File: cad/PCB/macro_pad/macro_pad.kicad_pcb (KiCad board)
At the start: 2 copper layers, 82.3 x 100.8 mm, 39 parts, among them SW1 SW_Push, SW10 SW_Push, SW11 SW_Push, SW12 SW_Push, SW13 SW_Push, SW14 SW_Push, SW15 SW_Push, SW16 SW_Push, SW17 RotaryEncoder_Switch, SW2 SW_Push, SW3 SW_Push, SW4 SW_Push, SW5 SW_Push, SW6 SW_Push, SW7 SW_Push, SW8 SW_Push, SW9 SW_Push, U1 XIAO-SAMD21-DIP

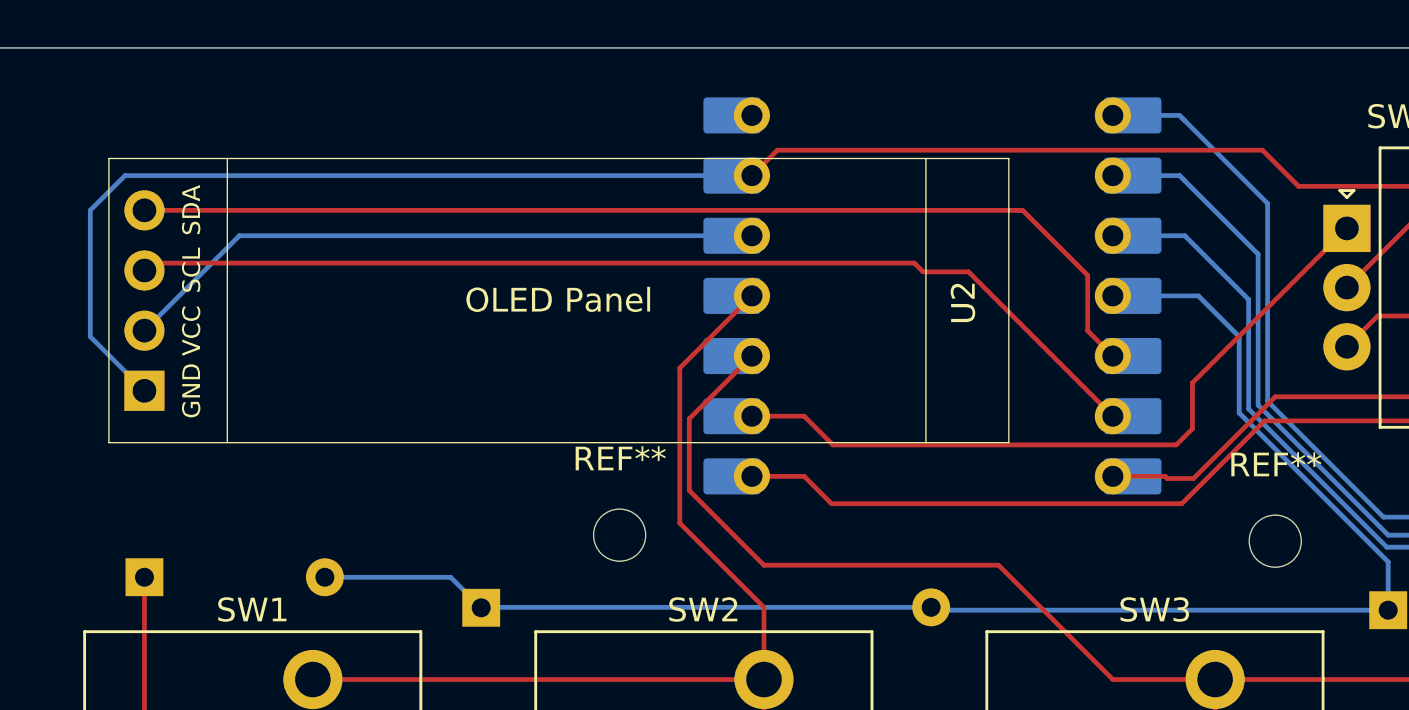
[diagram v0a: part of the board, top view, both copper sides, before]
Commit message: edited component placing added 3d models
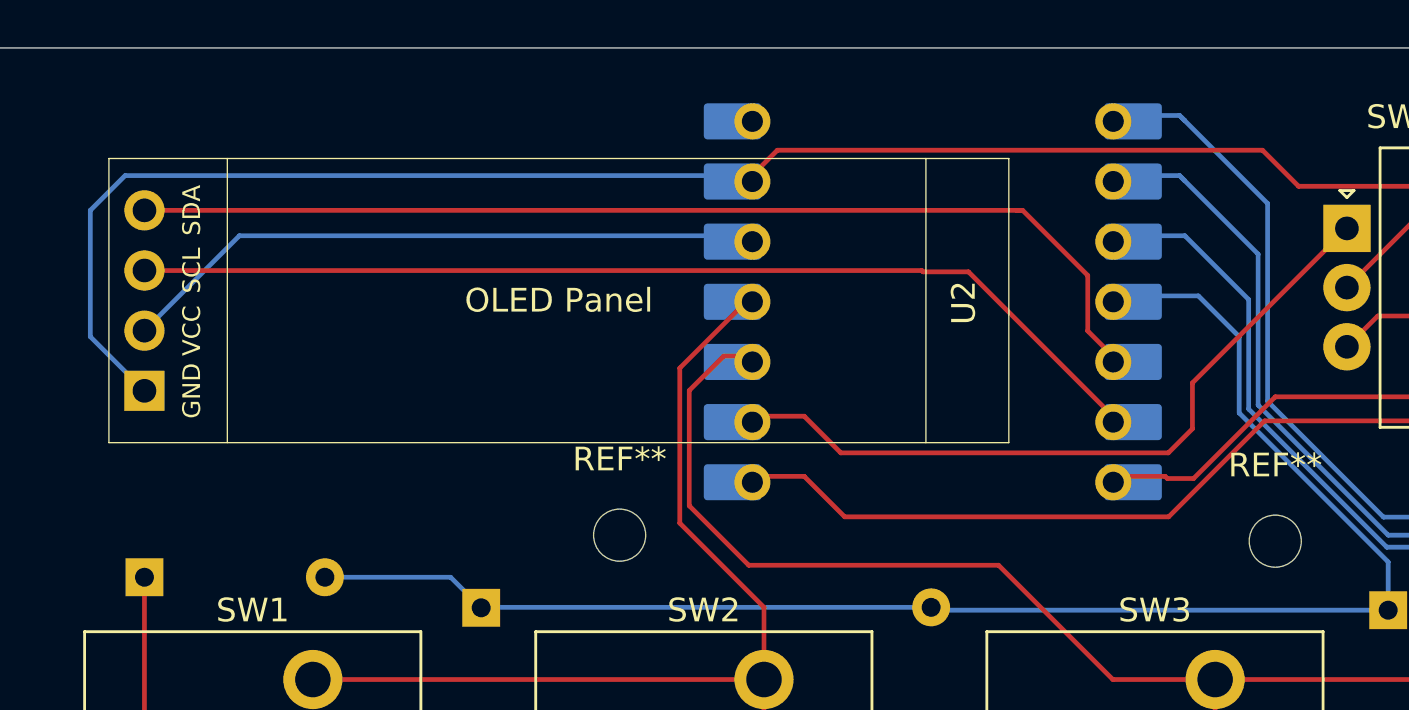
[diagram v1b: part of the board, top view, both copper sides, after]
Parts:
- moved U1 0.25 mm to (142.9, 74.2)
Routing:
- net Net-(U1-PA5_A9_D9_MISO): track 165.6 -> 166.7 mm
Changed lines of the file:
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@@
 			(outputformat 1)
 			(mirror no)
-			(drillshape 1)
+			(drillshape 0)
 			(scaleselection 1)
-			(outputdirectory "")
+			(outputdirectory "gerber/")
 		)
 	)
@@
 			(pintype "passive")
 		)
-		(model "${KICAD8_3DMODEL_DIR}/Rotary_Encoder.3dshapes/RotaryEncoder_Alps_EC11E-Switch_Vertical_H20mm.wrl"
+		(model "C:/Users/franc/Documents/KiCad/8.0/3dmodels/EC11_Rotary_Encoder_Switched.step"
 			(offset
-				(xyz 0 0 0)
+				(xyz 7.5 -2.5 0)
 			)
 			(scale
@@
 			)
 			(rotate
-				(xyz 0 0 0)
+				(xyz 0 0 90)
 			)
 		)
@@
 		(tags "Diode DO-35_SOD27 series Axial Horizontal pin pitch 7.62mm  length 4mm diameter 2mm")
 		(property "Reference" "D13"
-			(at 3.81 2.12 360)
+			(at 3.81 2.12 0)
 			(layer "B.SilkS")
 			(effects
@@
 		)
 		(property "Value" "D"
-			(at 3.81 -2.12 360)
+			(at 3.81 -2.12 0)
 			(layer "B.Fab")
 			(effects
@@
 		)
 		(fp_text user "K"
-			(at 0 1.8 360)
+			(at 0 1.8 0)
 			(layer "B.SilkS")
 			(effects
@@
 		)
 		(fp_text user "K"
-			(at 0 1.8 360)
+			(at 0 1.8 0)
 			(layer "B.Fab")
 			(effects
@@
 		)
 		(fp_text user "${REFERENCE}"
-			(at 4.11 0 360)
+			(at 4.11 0 0)
 			(layer "B.Fab")
 			(effects
@@
 		(tags "Diode DO-35_SOD27 series Axial Horizontal pin pitch 7.62mm  length 4mm diameter 2mm")
 		(property "Reference" "D1"
-			(at 3.81 2.12 360)
+			(at 3.81 2.12 0)
 			(layer "B.SilkS")
 			(effects
@@
 		)
 		(property "Value" "D"
-			(at 3.81 -2.12 360)
+			(at 3.81 -2.12 0)
 			(layer "B.Fab")
 			(effects
@@
 		)
 		(fp_text user "K"
-			(at 0 1.8 360)
+			(at 0 1.8 0)
 			(layer "B.SilkS")
 			(effects
@@
 		)
 		(fp_text user "K"
-			(at 0 1.8 360)
+			(at 0 1.8 0)
 			(layer "B.Fab")
 			(effects
@@
 		)
 		(fp_text user "${REFERENCE}"
-			(at 4.11 0 360)
+			(at 4.11 0 0)
 			(layer "B.Fab")
 			(effects
@@
 	(footprint "Seeed Studio XIAO Series Library:XIAO-SAMD21-DIP"
 		(layer "B.Cu")
-		(at 142.902 73.908 180)
+		(at 142.92 74.1575 180)
 		(property "Reference" "U1"
 			(at -8 12 0)
@@
 			)
 		)
-		(model "${AMZPATH}/3dmodels/AMz3D.3dshapes/Seeeduino XIAO SAMD21 v4.step"
+		(model "C:/Users/franc/Downloads/seeeduino-xiao-samd21-3d-model/Seeeduino XIAO SAMD21 v4.step"
 			(offset
 				(xyz 0 0 0)
@@
 			)
 			(rotate
-				(xyz 0 0 0)
+				(xyz 0 0 -90)
 			)
 		)
@@
 			)
 			(rotate
-				(xyz 0 0 90)
+				(xyz 90 0 90)
 			)
 		)
@@
 		(tags "Diode DO-35_SOD27 series Axial Horizontal pin pitch 7.62mm  length 4mm diameter 2mm")
 		(property "Reference" "D5"
-			(at 3.81 2.12 360)
+			(at 3.81 2.12 0)
 			(layer "B.SilkS")
 			(effects
@@
 		)
 		(property "Value" "D"
-			(at 3.81 -2.12 360)
+			(at 3.81 -2.12 0)
 			(layer "B.Fab")
 			(effects
@@
 		)
 		(fp_text user "K"
-			(at 0 1.8 360)
+			(at 0 1.8 0)
 			(layer "B.SilkS")
 			(effects
@@
 		)
 		(fp_text user "K"
-			(at 0 1.8 360)
+			(at 0 1.8 0)
 			(layer "B.Fab")
 			(effects
@@
 		)
 		(fp_text user "${REFERENCE}"
-			(at 4.11 0 360)
+			(at 4.11 0 0)
 			(layer "B.Fab")
 			(effects
@@
 		(tags "Diode DO-35_SOD27 series Axial Horizontal pin pitch 7.62mm  length 4mm diameter 2mm")
 		(property "Reference" "D9"
-			(at 3.81 2.12 360)
+			(at 3.81 2.12 0)
 			(layer "B.SilkS")
 			(effects
@@
 		)
 		(property "Value" "D"
-			(at 3.81 -2.12 360)
+			(at 3.81 -2.12 0)
 			(layer "B.Fab")
 			(effects
@@
 		)
 		(fp_text user "K"
-			(at 0 1.8 360)
+			(at 0 1.8 0)
 			(layer "B.SilkS")
 			(effects
@@
 		)
 		(fp_text user "K"
-			(at 0 1.8 360)
+			(at 0 1.8 0)
 			(layer "B.Fab")
 			(effects
@@
 		)
 		(fp_text user "${REFERENCE}"
-			(at 4.11 0 360)
+			(at 4.11 0 0)
 			(layer "B.Fab")
 			(effects
@@
 	)
 	(segment
+		(start 135.244 85.344)
+		(end 132.734 82.834)
+		(width 0.2)
+		(layer "F.Cu")
+		(net 20)
+	)
+	(segment
 		(start 154.94 128.27)
 		(end 154.94 147.32)
@@
 	)
 	(segment
-		(start 173.99 147.32)
-		(end 154.94 147.32)
+		(start 132.734 77.966)
+		(end 134.1895 76.5105)
 		(width 0.2)
 		(layer "F.Cu")
@@
 	)
 	(segment
-		(start 132.734 79.1585)
-		(end 135.382 76.5105)
+		(start 173.99 147.32)
+		(end 154.94 147.32)
 		(width 0.2)
 		(layer "F.Cu")
@@
 	)
 	(segment
-		(start 132.734 82.188)
-		(end 132.734 79.1585)
+		(start 173.99 90.17)
+		(end 154.94 90.17)
 		(width 0.2)
 		(layer "F.Cu")
@@
 	)
 	(segment
-		(start 173.99 90.17)
-		(end 154.94 90.17)
+		(start 150.622 90.17)
+		(end 145.796 85.344)
 		(width 0.2)
 		(layer "F.Cu")
@@
 	)
 	(segment
-		(start 135.89 85.344)
-		(end 132.734 82.188)
+		(start 145.796 85.344)
+		(end 135.244 85.344)
 		(width 0.2)
 		(layer "F.Cu")
@@
 	)
 	(segment
-		(start 150.622 90.17)
-		(end 145.796 85.344)
+		(start 134.1895 76.5105)
+		(end 135.382 76.5105)
 		(width 0.2)
 		(layer "F.Cu")
@@
 	)
 	(segment
-		(start 145.796 85.344)
-		(end 135.89 85.344)
+		(start 173.99 109.22)
+		(end 154.94 109.22)
 		(width 0.2)
 		(layer "F.Cu")
@@
 	)
 	(segment
-		(start 173.99 109.22)
-		(end 154.94 109.22)
+		(start 132.734 82.834)
+		(end 132.734 77.966)
 		(width 0.2)
 		(layer "F.Cu")
@@
 	)
 	(segment
-		(start 157.029686 79.248)
-		(end 153.533186 82.7445)
+		(start 175.494478 77.47)
+		(end 166.612 77.47)
 		(width 0.2)
 		(layer "F.Cu")
@@
 	)
 	(segment
-		(start 153.533186 82.7445)
-		(end 138.742 82.7445)
+		(start 164.834 79.248)
+		(end 157.029686 79.248)
 		(width 0.2)
 		(layer "F.Cu")
@@
 	)
 	(segment
-		(start 164.834 79.248)
-		(end 157.029686 79.248)
+		(start 160.506 76.12)
+		(end 161.806 74.82)
 		(width 0.2)
 		(layer "F.Cu")
@@
 	)
 	(segment
-		(start 175.544478 74.82)
-		(end 176.306 75.581522)
+		(start 176.306 76.658478)
+		(end 175.494478 77.47)
 		(width 0.2)
 		(layer "F.Cu")
@@
 	)
 	(segment
-		(start 160.506 76.12)
-		(end 161.806 74.82)
+		(start 166.612 77.47)
+		(end 164.834 79.248)
 		(width 0.2)
 		(layer "F.Cu")
@@
 	)
 	(segment
-		(start 137.588 81.5905)
-		(end 135.382 81.5905)
+		(start 175.544478 74.82)
+		(end 176.306 75.581522)
 		(width 0.2)
 		(layer "F.Cu")
@@
 	)
 	(segment
-		(start 138.742 82.7445)
-		(end 137.588 81.5905)
+		(start 157.029686 79.248)
+		(end 152.977686 83.3)
 		(width 0.2)
 		(layer "F.Cu")
@@
 	)
 	(segment
-		(start 176.306 76.658478)
-		(end 175.494478 77.47)
+		(start 139.2975 83.3)
+		(end 137.588 81.5905)
 		(width 0.2)
 		(layer "F.Cu")
@@
 	)
 	(segment
-		(start 175.494478 77.47)
-		(end 166.612 77.47)
+		(start 152.977686 83.3)
+		(end 139.2975 83.3)
 		(width 0.2)
 		(layer "F.Cu")
@@
 	)
 	(segment
-		(start 166.612 77.47)
-		(end 164.834 79.248)
+		(start 137.588 81.5905)
+		(end 135.382 81.5905)
 		(width 0.2)
 		(layer "F.Cu")
@@
 	)
 	(segment
-		(start 160.506 71.12)
-		(end 153.982 77.644)
+		(start 137.588 79.0505)
+		(end 135.382 79.0505)
 		(width 0.2)
 		(layer "F.Cu")
@@
 	)
 	(segment
-		(start 135.382 79.0505)
-		(end 137.588 79.0505)
+		(start 152.964395 80.6)
+		(end 139.1375 80.6)
 		(width 0.2)
 		(layer "F.Cu")
@@
 	)
 	(segment
-		(start 137.588 79.0505)
-		(end 138.8015 80.264)
+		(start 160.506 71.12)
+		(end 153.982 77.644)
 		(width 0.2)
 		(layer "F.Cu")
@@
 	)
 	(segment
-		(start 153.300395 80.264)
-		(end 138.8015 80.264)
+		(start 153.982 77.644)
+		(end 153.982 79.582395)
 		(width 0.2)
 		(layer "F.Cu")
@@
 	)
 	(segment
-		(start 153.982 77.644)
-		(end 153.982 79.582395)
+		(start 153.982 79.582395)
+		(end 152.964395 80.6)
 		(width 0.2)
 		(layer "F.Cu")
@@
 	)
 	(segment
-		(start 153.982 79.582395)
-		(end 153.300395 80.264)
+		(start 139.1375 80.6)
+		(end 137.588 79.0505)
 		(width 0.2)
 		(layer "F.Cu")
@@
 	)
 	(segment
-		(start 150.622 79.0505)
-		(end 144.526 72.9545)
+		(start 109.73 72.9)
+		(end 109.728 72.898)
 		(width 0.2)
 		(layer "F.Cu")
@@
 	)
 	(segment
-		(start 142.24 72.5845)
-		(end 110.0415 72.5845)
+		(start 142.61 72.9545)
+		(end 142.5555 72.9)
 		(width 0.2)
 		(layer "F.Cu")
@@
 	)
 	(segment
-		(start 110.0415 72.5845)
-		(end 109.728 72.898)
+		(start 142.5555 72.9)
+		(end 109.73 72.9)
 		(width 0.2)
 		(layer "F.Cu")
@@
 	)
 	(segment
-		(start 144.526 72.9545)
-		(end 142.61 72.9545)
+		(start 150.622 79.0505)
+		(end 144.526 72.9545)
 		(width 0.2)
 		(layer "F.Cu")
@@
 	)
 	(segment
-		(start 142.61 72.9545)
-		(end 142.24 72.5845)
+		(start 144.526 72.9545)
+		(end 142.61 72.9545)
 		(width 0.2)
 		(layer "F.Cu")
